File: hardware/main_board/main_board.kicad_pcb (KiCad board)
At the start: 2 copper layers, 95.3 x 71.6 mm, 77 parts, among them IC1 E22-900M22S, IC2 INA226AIDGST, IC3 INA226AIDGST, IC4 TPS2121RUXT, IC5 TP5000-QFN16, J2 I2C External Modules, J3 Solar panel, J5 Battary over BMS, J6 USB4105-GF-A-060, U1 ESP32-C3-WROOM-02, U2 DS3231SN, U4 TPS631000DRLR

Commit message: hw v1
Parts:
- added G***: LOGO, LOGO, F.Cu at (138.3, 66.3)
- added REF**: MountingHole_3.2mm_M3, MountingHole:MountingHole_3.2mm_M3, F.Cu at (78.4, 105.8)
- added REF**: MountingHole_3.2mm_M3, MountingHole:MountingHole_3.2mm_M3, F.Cu at (164.3, 83.7)
- added REF**: MountingHole_3.2mm_M3, MountingHole:MountingHole_3.2mm_M3, F.Cu at (87.1, 45.7)
- added REF**: MountingHole_3.2mm_M3, MountingHole:MountingHole_3.2mm_M3, F.Cu at (161.0, 47.4)
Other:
- board text added: "(Literally)"
- board text added: "Cloud connected!"
- board text added: "METEO NODE REV V1 • 2026"
- board text added: "Якщо читаєш це - поверни назад у корпус."

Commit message: hw v1
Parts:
- moved REF3 40.8 mm to (192.7, 113.0)
- moved REF2 38.7 mm to (192.0, 70.5)
- moved REF4 38.4 mm to (106.0, 132.5)
- moved R16 38.4 mm to (114.7, 83.7)
- moved AE1 38.4 mm to (189.4, 94.2)
- moved BT1 38.4 mm to (178.0, 125.0)
- moved C1 38.4 mm to (116.1, 114.8)
- moved C11 38.4 mm to (133.4, 70.9)
- moved C17 38.4 mm to (145.5, 75.3)
- moved C2 38.4 mm to (117.6, 114.8)
- moved C21 38.4 mm to (149.9, 124.2)
- moved C6 38.4 mm to (120.7, 114.8)
- moved C8 38.4 mm to (170.1, 121.2)
- moved D1 38.4 mm to (160.4, 114.6)
- moved G*** 38.4 mm to (166.0, 93.0)
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- renumbered REF** to REF1, REF** to REF2, REF** to REF3, REF** to REF4

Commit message: hw gerber files
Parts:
- moved TP9 3.29 mm to (109.2, 73.5)
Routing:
- net GND: vias 33 -> 22
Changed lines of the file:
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@@
 	(footprint "TestPoint:TestPoint_Pad_D1.0mm"
 		(layer "F.Cu")
-		(at 108.5956 70.306)
+		(at 109.22 73.533)
 		(descr "SMD pad as test Point, diameter 1.0mm")
 		(tags "test point SMD pad")
@@
 	)
 	(gr_text "(Literally)"
-		(at 153.162 101.473 0)
+		(at 153.543 101.473 0)
 		(layer "F.SilkS")
 		(effects
@@
 	)
 	(gr_text "Cloud connected!"
-		(at 133.35 101.727 0)
+		(at 133.731 101.727 0)
 		(layer "F.SilkS")
 		(effects
@@
 	)
 	(via
-		(at 176.53 115.443)
-		(size 0.6)
-		(drill 0.3)
-		(layers "F.Cu" "B.Cu")
-		(free yes)
-		(net "GND")
-	)
-	(via
 		(at 154.432 71.12)
 		(size 0.6)
@@
 	)
 	(via
-		(at 159.385 80.645)
-		(size 0.6)
-		(drill 0.3)
-		(layers "F.Cu" "B.Cu")
-		(free yes)
-		(net "GND")
-	)
-	(via
 		(at 120.65 116.332)
 		(size 0.6)
@@
 	)
 	(via
-		(at 124.587 109.347)
-		(size 0.6)
-		(drill 0.3)
-		(layers "F.Cu" "B.Cu")
-		(free yes)
-		(net "GND")
-	)
-	(via
 		(at 139.1264 120.3694)
 		(size 0.6)
@@
 	)
 	(via
-		(at 118.999 91.186)
-		(size 0.6)
-		(drill 0.3)
-		(layers "F.Cu" "B.Cu")
-		(free yes)
-		(net "GND")
-	)
-	(via
 		(at 171.704 69.342)
 		(size 0.6)
@@
 	)
 	(via
-		(at 140.716 106.553)
-		(size 0.6)
-		(drill 0.3)
-		(layers "F.Cu" "B.Cu")
-		(free yes)
-		(net "GND")
-	)
-	(via
 		(at 122.174 80.264)
 		(size 0.6)
@@
 	)
 	(via
-		(at 158.115 106.68)
-		(size 0.6)
-		(drill 0.3)
-		(layers "F.Cu" "B.Cu")
-		(free yes)
-		(net "GND")
-	)
-	(via
 		(at 150.368 113.284)
 		(size 0.6)
@@
 	)
 	(via
-		(at 121.539 107.95)
-		(size 0.6)
-		(drill 0.3)
-		(layers "F.Cu" "B.Cu")
-		(free yes)
-		(net "GND")
-	)
-	(via
-		(at 160.528 69.215)
-		(size 0.6)
-		(drill 0.3)
-		(layers "F.Cu" "B.Cu")
-		(free yes)
-		(net "GND")
-	)
-	(via
 		(at 137.9834 116.5594)
 		(size 0.6)
@@
 	)
 	(via
-		(at 125.857 85.852)
-		(size 0.6)
-		(drill 0.3)
-		(layers "F.Cu" "B.Cu")
-		(free yes)
-		(net "GND")
-	)
-	(via
 		(at 112.903 85.852)
 		(size 0.6)
@@
 		(net "GND")
 	)
-	(via
-		(at 148.463 106.934)
-		(size 0.6)
-		(drill 0.3)
-		(layers "F.Cu" "B.Cu")
-		(free yes)
-		(net "GND")
-	)
-	(via
-		(at 130.302 133.096)
-		(size 0.6)
-		(drill 0.3)
-		(layers "F.Cu" "B.Cu")
-		(free yes)
-		(net "GND")
-	)

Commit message: hw v1 add sw
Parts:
- added J1: power swith, Connector_JST:JST_XH_B2B-XH-A_1x02_P2.50mm_Vertical, F.Cu at (127.8, 129.9)
- TP7: value TP_BAT_SYSTEM -> TP_BAT_SW
- moved TP4 1.97 mm to (131.4, 123.1)
- moved R19 1.82 mm to (126.1, 123.4), turned to 180 degrees
- moved TP11 0.76 mm to (123.7, 120.5)
- moved R26 0.08 mm to (146.4, 133.3)
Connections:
- C22 pad 1: BAT_SYSTEM -> /Power/BAT_SW
- IC5 pad 9: BAT_SYSTEM -> /Power/BAT_SW
- R19 pad 1: BAT_SYSTEM -> /Power/BAT_SW
- R21 pad 1: BAT_SYSTEM -> /Power/BAT_SW
- TP7 pad 1: BAT_SYSTEM -> /Power/BAT_SW
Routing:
- net /Power/BAT_SW: track 0.00 -> 39.8 mm, vias 0 -> 2
- net BAT_SYSTEM: track 44.1 -> 30.5 mm, vias 0 -> 1
- net BAT_FUSED: track 33.3 -> 37.1 mm
- net /Power/NTC_SENSE: track 45.3 -> 48.2 mm
- net GND: track 42.4 -> 43.7 mm

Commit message: hw v1 cleanup
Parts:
- TP10: value ESP32_BOOT -> BOOT
- TP6: value ESP32_EN -> EN
- moved TP5 2.16 mm to (117.1, 78.2)
- moved R3 2.07 mm to (168.3, 87.8)
- moved F1 0.91 mm to (119.6, 124.1)
- moved TP3 0.78 mm to (122.9, 126.5)
- moved TP11 0.65 mm to (123.8, 119.9)
- moved U4 0.19 mm to (137.3, 120.0)
- moved TP6 0.13 mm to (127.0, 117.9)
- moved R25 0.07 mm to (140.3, 119.2)
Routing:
- net GND: track 43.7 -> 41.2 mm
- net +3V3: track 281.0 -> 278.8 mm
- net /main_board/LORA_NSS: track 51.2 -> 53.0 mm
- net BAT_FUSED: track 37.1 -> 38.3 mm
- net /Power/BAT_RAW: track 8.16 -> 7.22 mm
- net SOLAR_IN: track 16.9 -> 17.6 mm
- net /Power/USB_5V: track 55.5 -> 56.1 mm

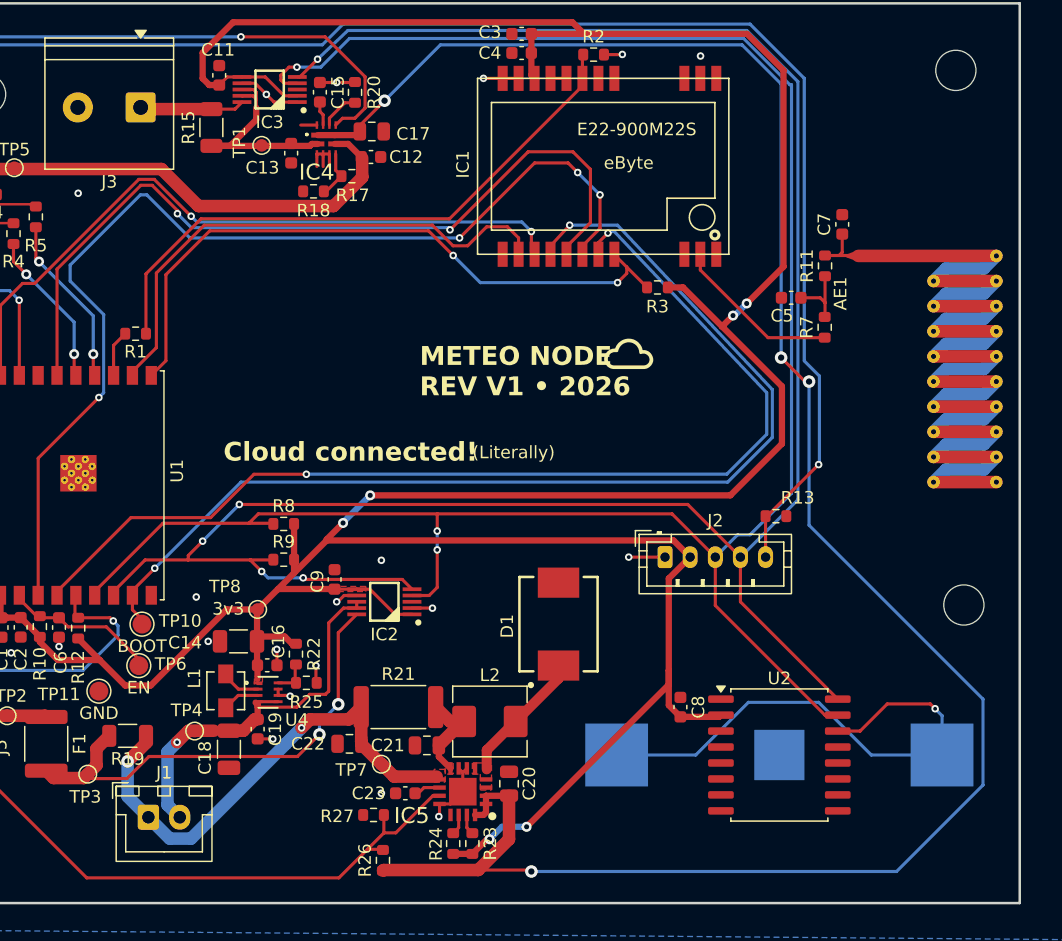
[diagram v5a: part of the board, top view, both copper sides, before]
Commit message: hw v1 add PCA9536DR
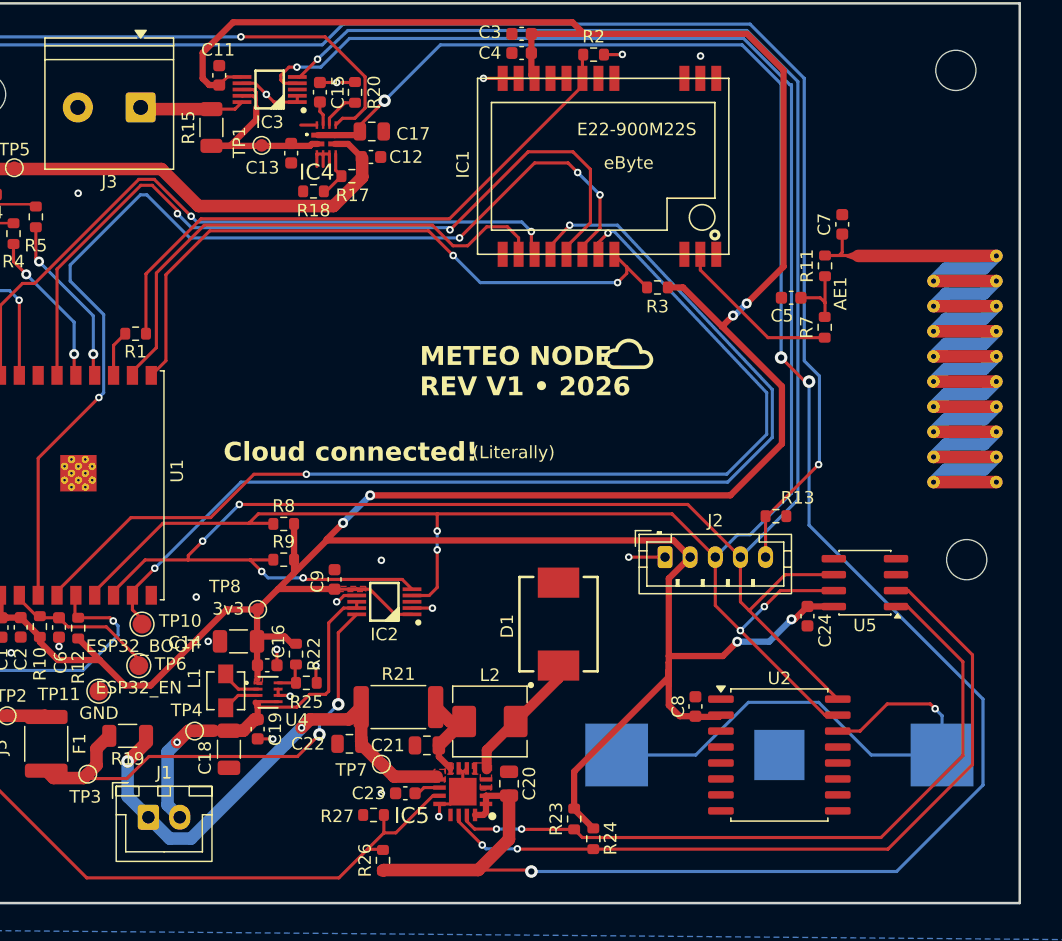
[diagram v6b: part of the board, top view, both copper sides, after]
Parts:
- added C24: 100nF, Capacitor_SMD:C_0603_1608Metric, F.Cu at (180.2, 113.9)
- added U5: PCA9536DR, Package_SO:SOIC-8_3.9x4.9mm_P1.27mm, F.Cu at (184.8, 111.3)
- TP10: value BOOT -> ESP32_BOOT
- TP6: value EN -> ESP32_EN
- moved R24 11.2 mm to (163.2, 131.6), turned to 90 degrees
- moved R23 8.33 mm to (161.6, 130.1), turned to 90 degrees
- moved REF3 3.61 mm to (192.9, 109.4)
- moved C8 1.20 mm to (171.3, 121.1)
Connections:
- IC3 pad 2: +3V3 -> GND
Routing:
- net STDBY_STATUS: track 1.63 -> 62.0 mm, vias 0 -> 2
- net CHRG_STATUS: track 1.63 -> 57.8 mm, vias 0 -> 2
- net /main_board/I2C_SDA: track 166.8 -> 175.6 mm, vias 3 -> 5
- net /main_board/I2C_SCL: track 172.9 -> 180.8 mm
- net +3V3: track 278.8 -> 282.8 mm
- net GND: track 41.2 -> 41.7 mm

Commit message: hw v1 resize board
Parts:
- moved REF4 0.34 mm to (106.0, 132.8)
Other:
- board size 95.3 x 71.6 mm -> 96 x 72 mm
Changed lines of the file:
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@@
 	(footprint "MountingHole:MountingHole_3.2mm_M3"
 		(layer "F.Cu")
-		(at 106.045 132.461)
+		(at 105.9688 132.7912)
 		(descr "Mounting Hole 3.2mm, M3, no annular, generated by kicad-footprint-generator mountinghole.py")
 		(tags "mountinghole M3")
@@
 	(gr_rect
 		(start 101.7884 65.151)
-		(end 197.104 136.7524)
+		(end 197.7884 137.151)
 		(stroke
 			(width 0.2)
@@
 	)
 	(gr_text "Якщо читаєш це - поверни назад у корпус."
-		(at 143.764 135.128 0)
+		(at 144.2212 135.7376 0)
 		(layer "B.SilkS")
 		(effects
